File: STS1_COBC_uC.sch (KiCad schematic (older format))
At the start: 27 parts

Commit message: RF modules added + some tweaking on STM32
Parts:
- removed D? (x6): LED, symbol Device:LED
- removed R? (x6): 52.5, symbol Device:R
- added C? (x2): 4.7u, symbol Device:C
- added C? (x5): 100n, symbol Device:C
- added C? (x2): 20p, symbol Device:C
- added C?: 1u, symbol Device:C
- added J? (x8): Conn_01x01_Male, symbol Connector:Conn_01x01_Male
- added JP?: Jumper_NC_Dual, symbol Device:Jumper_NC_Dual
- added R?: 220, symbol Device:R
- added Y?: 12MHz, symbol Device:Crystal
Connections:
- net labels added: GND, SPI1_CLK, SPI1_MISO, SPI1_MOSI, SPI2_CLK, SPI2_MISO, SPI2_MOSI, SPI3_MISO, SPI3_MOSI, SPI3_NSS, SPI3_SCLK, STM32_PowerSupply1, STM32_PowerSupply2, STM32_PowerSupply3, STM32_PowerSupply4
- net labels removed: Earth
- wire segments 41 -> 113
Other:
- note added: "Boot0 / Boot1 Bootloaderconfig\n"
- note added: "PA4 SPI3 NSS\nPA5 SPI1 SCLK\nPA6 SPI1 MISO\nPA7 SPI1 MOSI\nPA13 SWDIO\nPA14 SWCLK\nPB12 SPI3 SCKL\nPC2 SPI2 MISO\nPC3 SPI2 MOSI\nPC7 SPI2 SCLK\nPC11 SPI3 MISO\nPC12 SPI3 MOSI\n\nunbedingt spis wegen nss prüfen\n"
- note added: "Will be connected via jumpers\n"
- note removed: "PA5 SPI1 SCLK\nPA6 SPI1 MISO\nPA7 SPI1 MOSI\nPA13 SWDIO\nPA14 SWCLK\nPC2 SPI2 MISO\nPC3 SPI2 MOSI\nPC7 SPI2 SCLK\n\n"
- moved on the sheet: D?, J?, R?

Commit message: finished schematic
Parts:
- removed J? (x2): Conn_01x02_Female, symbol Connector:Conn_01x02_Female
- added J11, J15, J19, J22, J4: Conn_01x01_Male, symbol Connector:Conn_01x01_Male
- added J2: Conn_01x05_Female, Connector_PinHeader_2.54mm:PinHeader_1x05_P2.54mm_Horizontal, symbol Connector:Conn_01x05_Female
- C1, C10, C2, C3, C4, C5, C6, C7, C8, C9: renamed from C?; footprint (none) -> Capacitor_SMD:C_0805_2012Metric
- D1, D2: renamed from D?; footprint (none) -> LED_SMD:LED_0805_2012Metric
- IC1: renamed from IC?; footprint QFP50P1200X1200X160-64N -> STM32F411RET6TR:QFP50P1200X1200X160-64N
- R2, R3: renamed from R?; value 52.5 -> 100
- gave numbers to parts that had none: 19
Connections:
- net GND: now also J2.3 (Pin_3); no longer J7.1 (Pin_1)
- net SPI3_SCLK: now also IC1.51 (PC10), J15.1 (Pin_1); no longer IC1.33 (PB12), J20.1 (Pin_1)
- net STM32_PowerSupply4: now also J2.1 (Pin_1)
- net SPI4_MOSI: now reaches IC1.15 (PA1)
- net SPI4_MOSI: now also J4.1 (Pin_1)
- net STM32_PowerSupply1: now reaches C5.2, IC1.19 (VDD_1)
- net STM32_PowerSupply1: now also J7.1 (Pin_1)
- net SPI4_SCLK: now reaches IC1.34 (PB13)
- net SPI4_SCLK: now also J19.1 (Pin_1)
- net STM32_PA9(Watchdog_toggle): now reaches IC1.42 (PA9)
- net SPI4_MISO: now reaches IC1.44 (PA11)
- net SPI4_MISO: now also J22.1 (Pin_1)
- net at IC1.46 (PA13), J23.1 (Pin_1), R3.2: now also J2.4 (Pin_4)
- net at IC1.49 (PA14), J17.1 (Pin_1), R2.2: now also J2.2 (Pin_2)
- net SPI2_NSS: now reaches IC1.62 (PB9)
- net SPI2_NSS: now also J11.1 (Pin_1)
- net STM32_NRST: now reaches IC1.7 (NRST)
- net STM32_NRST: now also J2.5 (Pin_5)
- new net SPI4_NSS: IC1.33 (PB12), J20.1 (Pin_1)
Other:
- note added: "PA1 SPI4 MOSI\nPA4 SPI3 NSS\nPA5 SPI1 SCLK\nPA6 SPI1 MISO\nPA7 SPI1 MOSI\nPA11 SPI4 MISO\nPA13 SWDIO\nPA14 SWCLK\nPB9 SPI2 NSS\nPB12 SPI4 NSS\nPB13 SPI4 SCLK\nPC2 SPI2 MISO\nPC3 SPI2 MOSI\nPC7 SPI2 SCLK\nPC10 SPI3 SCLK\nPC11 SPI3 MISO\nPC12 SPI3 MOSI\n\nunbedingt spis wegen nss prüfen\n"
- note removed: "PA4 SPI3 NSS\nPA5 SPI1 SCLK\nPA6 SPI1 MISO\nPA7 SPI1 MOSI\nPA13 SWDIO\nPA14 SWCLK\nPB12 SPI3 SCKL\nPC2 SPI2 MISO\nPC3 SPI2 MOSI\nPC7 SPI2 SCLK\nPC11 SPI3 MISO\nPC12 SPI3 MOSI\n\nunbedingt spis wegen nss prüfen\n"

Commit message: new template
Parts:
- J10, J11, J12, J13, J14, J15, J16, J17, J18, J19, J20, J21, J22, J23, J3, J4, J5, J6, J7, J8, J9: footprint (none) -> Connector_PinHeader_2.54mm:PinHeader_1x01_P2.54mm_Vertical
- R1, R2, R3: footprint (none) -> Resistor_SMD:R_0805_2012Metric
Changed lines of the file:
@@
 F 0 "J5" V 4612 3794 50  0000 L CNN
 F 1 "Conn_01x01_Male" V 4703 3794 50  0000 L CNN
-F 2 "" H 4550 3750 50  0001 C CNN
+F 2 "Connector_PinHeader_2.54mm:PinHeader_1x01_P2.54mm_Vertical" H 4550 3750 50  0001 C CNN
 F 3 "~" H 4550 3750 50  0001 C CNN
 	1    4550 3750
@@
 F 0 "J6" V 4704 4162 50  0000 R CNN
 F 1 "Conn_01x01_Male" V 4613 4162 50  0000 R CNN
-F 2 "" H 4550 4250 50  0001 C CNN
+F 2 "Connector_PinHeader_2.54mm:PinHeader_1x01_P2.54mm_Vertical" H 4550 4250 50  0001 C CNN
 F 3 "~" H 4550 4250 50  0001 C CNN
 	1    4550 4250
@@
 F 0 "J9" H 5408 5681 50  0000 C CNN
 F 1 "Conn_01x01_Male" H 5408 5590 50  0000 C CNN
-F 2 "" H 5300 5500 50  0001 C CNN
+F 2 "Connector_PinHeader_2.54mm:PinHeader_1x01_P2.54mm_Vertical" H 5300 5500 50  0001 C CNN
 F 3 "~" H 5300 5500 50  0001 C CNN
 	1    5300 5500
@@
 F 0 "J10" H 5508 5831 50  0000 C CNN
 F 1 "Conn_01x01_Male" H 5508 5740 50  0000 C CNN
-F 2 "" H 5400 5650 50  0001 C CNN
+F 2 "Connector_PinHeader_2.54mm:PinHeader_1x01_P2.54mm_Vertical" H 5400 5650 50  0001 C CNN
 F 3 "~" H 5400 5650 50  0001 C CNN
 	1    5400 5650
@@
 F 0 "J12" H 5872 5482 50  0000 R CNN
 F 1 "Conn_01x01_Male" H 6200 5600 50  0000 R CNN
-F 2 "" H 5900 5550 50  0001 C CNN
+F 2 "Connector_PinHeader_2.54mm:PinHeader_1x01_P2.54mm_Vertical" H 5900 5550 50  0001 C CNN
 F 3 "~" H 5900 5550 50  0001 C CNN
 	1    5900 5550
@@
 F 0 "J21" V 7262 3894 50  0000 L CNN
 F 1 "Conn_01x01_Male" V 7353 3894 50  0000 L CNN
-F 2 "" H 7200 3850 50  0001 C CNN
+F 2 "Connector_PinHeader_2.54mm:PinHeader_1x01_P2.54mm_Vertical" H 7200 3850 50  0001 C CNN
 F 3 "~" H 7200 3850 50  0001 C CNN
 	1    7200 3850
@@
 F 0 "J23" V 7462 2944 50  0000 L CNN
 F 1 "Conn_01x01_Male" V 7553 2944 50  0000 L CNN
-F 2 "" H 7400 2900 50  0001 C CNN
+F 2 "Connector_PinHeader_2.54mm:PinHeader_1x01_P2.54mm_Vertical" H 7400 2900 50  0001 C CNN
 F 3 "~" H 7400 2900 50  0001 C CNN
 	1    7400 2900
@@
 F 0 "J17" H 6772 2182 50  0000 R CNN
 F 1 "Conn_01x01_Male" V 6750 2600 50  0000 R CNN
-F 2 "" H 6800 2250 50  0001 C CNN
+F 2 "Connector_PinHeader_2.54mm:PinHeader_1x01_P2.54mm_Vertical" H 6800 2250 50  0001 C CNN
 F 3 "~" H 6800 2250 50  0001 C CNN
 	1    6800 2250
@@
 F 0 "R2" H 6650 2000 50  0000 L CNN
 F 1 "100" V 6600 1900 50  0000 L CNN
-F 2 "" V 6530 2000 50  0001 C CNN
+F 2 "Resistor_SMD:R_0805_2012Metric" V 6530 2000 50  0001 C CNN
 F 3 "~" H 6600 2000 50  0001 C CNN
 	1    6600 2000
@@
 F 0 "R3" H 7820 2996 50  0000 L CNN
 F 1 "100" H 7820 2905 50  0000 L CNN
-F 2 "" V 7680 2950 50  0001 C CNN
+F 2 "Resistor_SMD:R_0805_2012Metric" V 7680 2950 50  0001 C CNN
 F 3 "~" H 7750 2950 50  0001 C CNN
 	1    7750 2950
@@
 F 0 "J7" H 4908 5681 50  0000 C CNN
 F 1 "Conn_01x01_Male" H 4908 5590 50  0000 C CNN
-F 2 "" H 4800 5500 50  0001 C CNN
+F 2 "Connector_PinHeader_2.54mm:PinHeader_1x01_P2.54mm_Vertical" H 4800 5500 50  0001 C CNN
 F 3 "~" H 4800 5500 50  0001 C CNN
 	1    4800 5500
@@
 F 0 "J18" H 7050 5600 50  0000 C CNN
 F 1 "Conn_01x01_Male" H 6650 5600 50  0000 C CNN
-F 2 "" H 7000 5600 50  0001 C CNN
+F 2 "Connector_PinHeader_2.54mm:PinHeader_1x01_P2.54mm_Vertical" H 7000 5600 50  0001 C CNN
 F 3 "~" H 7000 5600 50  0001 C CNN
 	1    7000 5600
@@
 F 0 "J16" V 6812 2894 50  0000 L CNN
 F 1 "Conn_01x01_Male" V 6750 2750 50  0000 L CNN
-F 2 "" H 6750 2850 50  0001 C CNN
+F 2 "Connector_PinHeader_2.54mm:PinHeader_1x01_P2.54mm_Vertical" H 6750 2850 50  0001 C CNN
 F 3 "~" H 6750 2850 50  0001 C CNN
 	1    6750 2850
@@
 F 0 "J8" H 4872 2032 50  0000 R CNN
 F 1 "Conn_01x01_Male" H 4872 2123 50  0000 R CNN
-F 2 "" H 4900 2100 50  0001 C CNN
+F 2 "Connector_PinHeader_2.54mm:PinHeader_1x01_P2.54mm_Vertical" H 4900 2100 50  0001 C CNN
 F 3 "~" H 4900 2100 50  0001 C CNN
 	1    4900 2100
@@
 F 0 "R1" H 3220 3796 50  0000 L CNN
 F 1 "220" V 3150 3650 50  0000 L CNN
-F 2 "" V 3080 3750 50  0001 C CNN
+F 2 "Resistor_SMD:R_0805_2012Metric" V 3080 3750 50  0001 C CNN
 F 3 "~" H 3150 3750 50  0001 C CNN
 	1    3150 3750
@@
 F 0 "J14" H 6072 2182 50  0000 R CNN
 F 1 "Conn_01x01_Male" H 6072 2273 50  0000 R CNN
-F 2 "" H 6100 2250 50  0001 C CNN
+F 2 "Connector_PinHeader_2.54mm:PinHeader_1x01_P2.54mm_Vertical" H 6100 2250 50  0001 C CNN
 F 3 "~" H 6100 2250 50  0001 C CNN
 	1    6100 2250
@@
 F 0 "J13" H 5972 2132 50  0000 R CNN
 F 1 "Conn_01x01_Male" H 5972 2223 50  0000 R CNN
-F 2 "" H 6000 2200 50  0001 C CNN
+F 2 "Connector_PinHeader_2.54mm:PinHeader_1x01_P2.54mm_Vertical" H 6000 2200 50  0001 C CNN
 F 3 "~" H 6000 2200 50  0001 C CNN
 	1    6000 2200
@@
 F 0 "J20" V 7112 4794 50  0000 L CNN
 F 1 "Conn_01x01_Male" V 7203 4794 50  0000 L CNN
-F 2 "" H 7050 4750 50  0001 C CNN
+F 2 "Connector_PinHeader_2.54mm:PinHeader_1x01_P2.54mm_Vertical" H 7050 4750 50  0001 C CNN
 F 3 "~" H 7050 4750 50  0001 C CNN
 	1    7050 4750
@@
 F 0 "J3" H 4508 6181 50  0000 C CNN
 F 1 "Conn_01x01_Male" H 4508 6090 50  0000 C CNN
-F 2 "" H 4400 6000 50  0001 C CNN
+F 2 "Connector_PinHeader_2.54mm:PinHeader_1x01_P2.54mm_Vertical" H 4400 6000 50  0001 C CNN
 F 3 "~" H 4400 6000 50  0001 C CNN
 	1    4400 6000
@@
 F 0 "J4" H 4608 5081 50  0000 C CNN
 F 1 "Conn_01x01_Male" H 4550 4900 50  0000 C CNN
-F 2 "" H 4500 4900 50  0001 C CNN
+F 2 "Connector_PinHeader_2.54mm:PinHeader_1x01_P2.54mm_Vertical" H 4500 4900 50  0001 C CNN
 F 3 "~" H 4500 4900 50  0001 C CNN
 	1    4500 4900
@@
 F 0 "J22" V 7362 3294 50  0000 L CNN
 F 1 "Conn_01x01_Male" V 7453 3294 50  0000 L CNN
-F 2 "" H 7300 3250 50  0001 C CNN
+F 2 "Connector_PinHeader_2.54mm:PinHeader_1x01_P2.54mm_Vertical" H 7300 3250 50  0001 C CNN
 F 3 "~" H 7300 3250 50  0001 C CNN
 	1    7300 3250
@@
 F 0 "J11" V 5562 2094 50  0000 L CNN
 F 1 "Conn_01x01_Male" V 5653 2094 50  0000 L CNN
-F 2 "" H 5500 2050 50  0001 C CNN
+F 2 "Connector_PinHeader_2.54mm:PinHeader_1x01_P2.54mm_Vertical" H 5500 2050 50  0001 C CNN
 F 3 "~" H 5500 2050 50  0001 C CNN
 	1    5500 2050
@@
 F 0 "J19" V 7112 4294 50  0000 L CNN
 F 1 "Conn_01x01_Male" V 7203 4294 50  0000 L CNN
-F 2 "" H 7050 4250 50  0001 C CNN
+F 2 "Connector_PinHeader_2.54mm:PinHeader_1x01_P2.54mm_Vertical" H 7050 4250 50  0001 C CNN
 F 3 "~" H 7050 4250 50  0001 C CNN
 	1    7050 4250
@@
 F 0 "J15" H 6172 2082 50  0000 R CNN
 F 1 "Conn_01x01_Male" H 6172 2173 50  0000 R CNN
-F 2 "" H 6200 2150 50  0001 C CNN
+F 2 "Connector_PinHeader_2.54mm:PinHeader_1x01_P2.54mm_Vertical" H 6200 2150 50  0001 C CNN
 F 3 "~" H 6200 2150 50  0001 C CNN
 	1    6200 2150
@@
 	6400 2150 6400 2350
 Connection ~ 6400 2150
-Text HLabel 4550 3650 0    50   Input ~ 0
-STM32_NRST
 Text HLabel 8400 3650 2    50   Input ~ 0
 STM32_PA9(Watchdog_toggle)
@@
 Wire Wire Line
 	4650 3650 4550 3650
+Text HLabel 4550 3650 0    50   Input ~ 0
+STM32_NRST
 $EndSCHEMATC

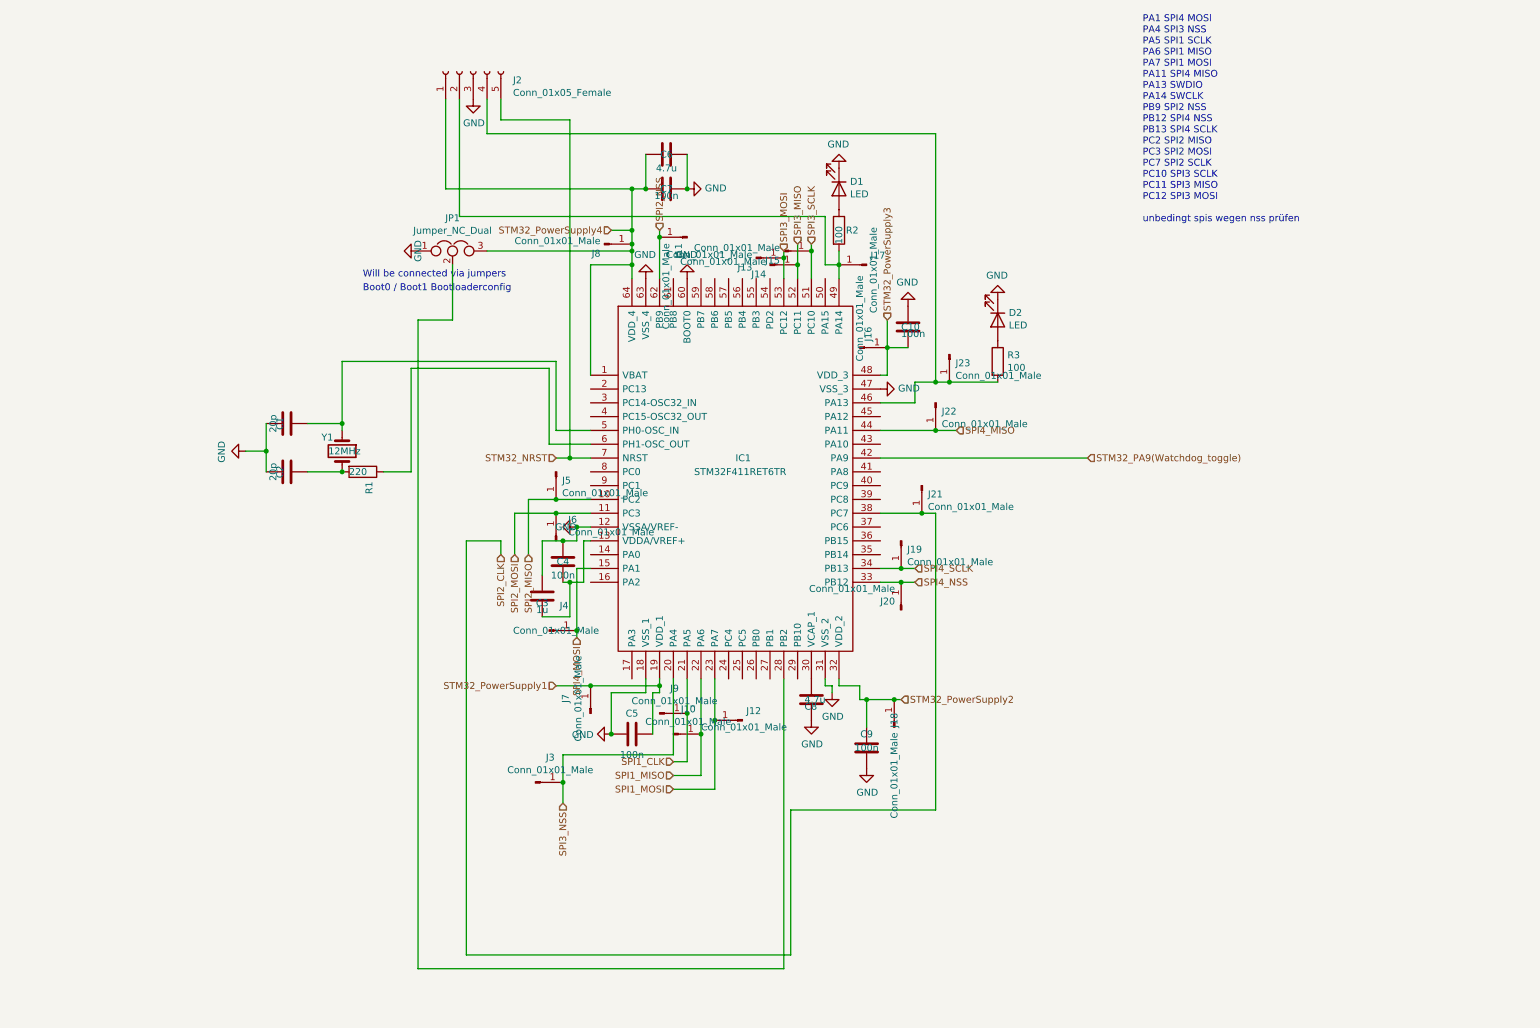
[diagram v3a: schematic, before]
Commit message: BuckBoost added
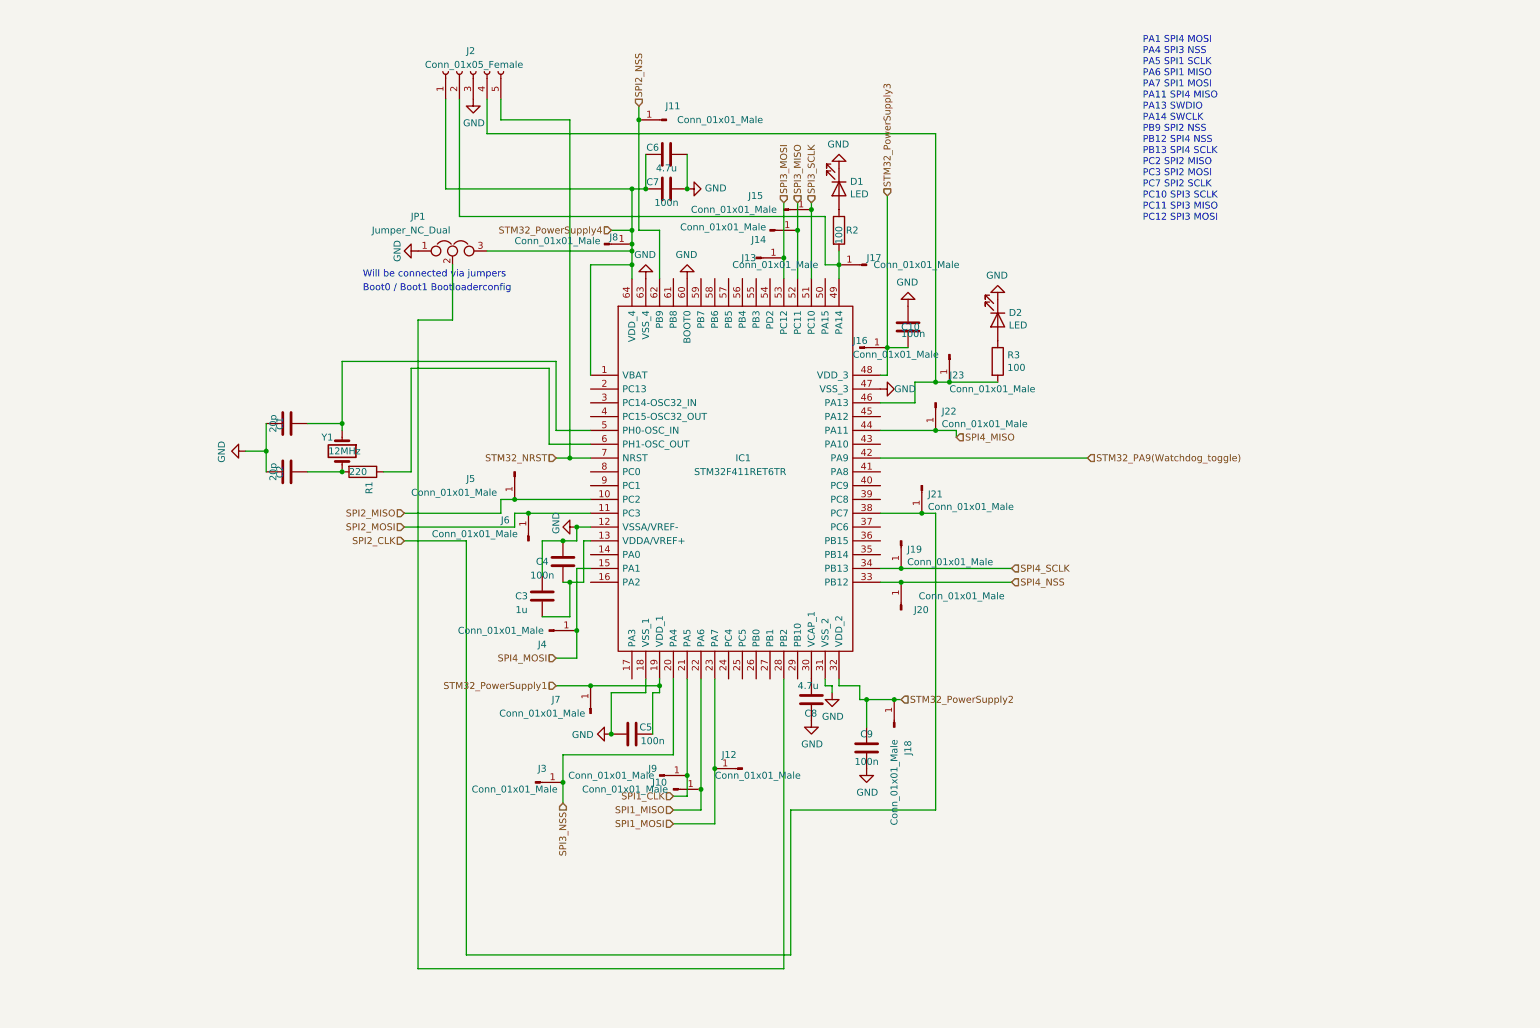
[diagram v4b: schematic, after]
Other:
- note added: "PA1 SPI4 MOSI\nPA4 SPI3 NSS\nPA5 SPI1 SCLK\nPA6 SPI1 MISO\nPA7 SPI1 MOSI\nPA11 SPI4 MISO\nPA13 SWDIO\nPA14 SWCLK\nPB9 SPI2 NSS\nPB12 SPI4 NSS\nPB13 SPI4 SCLK\nPC2 SPI2 MISO\nPC3 SPI2 MOSI\nPC7 SPI2 SCLK\nPC10 SPI3 SCLK\nPC11 SPI3 MISO\nPC12 SPI3 MOSI\n\n\n"
- note removed: "PA1 SPI4 MOSI\nPA4 SPI3 NSS\nPA5 SPI1 SCLK\nPA6 SPI1 MISO\nPA7 SPI1 MOSI\nPA11 SPI4 MISO\nPA13 SWDIO\nPA14 SWCLK\nPB9 SPI2 NSS\nPB12 SPI4 NSS\nPB13 SPI4 SCLK\nPC2 SPI2 MISO\nPC3 SPI2 MOSI\nPC7 SPI2 SCLK\nPC10 SPI3 SCLK\nPC11 SPI3 MISO\nPC12 SPI3 MOSI\n\nunbedingt spis wegen nss prüfen\n"
- moved on the sheet: J10, J11, J12, J14, J15, J5, J6, J9

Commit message: schematic done
final tweaks (adding LEDS, pin headers, moving circuits...)
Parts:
- added C?: 100n, Capacitor_SMD:C_0805_2012Metric, symbol Device:C
- added C?: 47u, Capacitor_SMD:C_0805_2012Metric, symbol Device:C
- added D?: LED, LED_SMD:LED_0805_2012Metric, symbol Device:LED
- added IC?: STWD100PYW83F, SamacSys_Parts:SOT65P210X110-5N, symbol SamacSys_Parts:STWD100PYW83F
- added J1, J26, J27, J28, J29, J30, J31, J32, J33, J34, J35, J36, J37, J38, J? (x15): Conn_01x01_Male, Connector_PinHeader_2.54mm:PinHeader_1x01_P2.54mm_Vertical, symbol Connector:Conn_01x01_Male
- added R?: 4k7, Resistor_SMD:R_0805_2012Metric, symbol Device:R
- added R?: 100, Resistor_SMD:R_0805_2012Metric, symbol Device:R
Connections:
- net GND: now also C?.2, C?.2, D?.1 (K), IC?.2 (GND), IC?.3 (~EN)
- net STM32_NRST: now also R?.2
- net STM32_PA9(Watchdog_toggle): now also IC?.4 (WDI), J?.1 (Pin_1)
- net at IC1.16 (PA2): now also J1.1 (Pin_1)
- net at IC1.17 (PA3): now also J26.1 (Pin_1)
- net PC13: now reaches IC1.2 (PC13)
- net PC13: now also J?.1 (Pin_1)
- net Flash_WP: now reaches IC1.24 (PC4)
- net at IC1.25 (PC5): now also J27.1 (Pin_1)
- net at IC1.26 (PB0): now also J28.1 (Pin_1)
- net at IC1.27 (PB1): now also J29.1 (Pin_1)
- net at IC1.29 (PB10): now also J30.1 (Pin_1)
- net PC14: now reaches IC1.3 (PC14-OSC32_IN)
- net PC14: now also J?.1 (Pin_1)
- net at IC1.35 (PB14): now also J38.1 (Pin_1)
- net at IC1.36 (PB15): now also J37.1 (Pin_1)
- net at IC1.37 (PC6): now also J36.1 (Pin_1)
- net at IC1.39 (PC8): now also J35.1 (Pin_1)
- net PC15: now reaches IC1.4 (PC15-OSC32_OUT)
- net PC15: now also J?.1 (Pin_1)
- net at IC1.40 (PC9): now also J34.1 (Pin_1)
- net at IC1.41 (PA8): now also J33.1 (Pin_1)
- net at IC1.43 (PA10): now also J32.1 (Pin_1)
- net at IC1.45 (PA12): now also J31.1 (Pin_1)
- net PA15: now reaches IC1.50 (PA15)
- net PA15: now also J?.1 (Pin_1)
- net PD2: now reaches IC1.54 (PD2)
- net PD2: now also J?.1 (Pin_1)
- net PB3: now reaches IC1.55 (PB3)
- net PB3: now also J?.1 (Pin_1)
- net PB4: now reaches IC1.56 (PB4)
- net PB4: now also J?.1 (Pin_1)
- net PB5: now reaches IC1.57 (PB5)
- net PB5: now also J?.1 (Pin_1)
- net PB6: now reaches IC1.58 (PB6)
- net PB6: now also J?.1 (Pin_1)
- net PB7: now reaches IC1.59 (PB7)
- net PB7: now also J?.1 (Pin_1)
- net PB9: now reaches IC1.61 (PB8)
- net PB9: now also J?.1 (Pin_1)
- net PC0: now reaches IC1.8 (PC0)
- net PC0: now also J?.1 (Pin_1)
- net PC1: now reaches IC1.9 (PC1)
- net PC1: now also J?.1 (Pin_1)
- new net: IC?.1 (~WDO), R?.1
- new net: D?.2 (A), R?.1
- new net Watchdog_VCC: C?.1, C?.1, IC?.5 (VCC), J?.1 (Pin_1), R?.2
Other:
- note added: "PA1 SPI4 MOSI\nPA4 SPI3 NSS\nPA5 SPI1 SCLK\nPA6 SPI1 MISO\nPA7 SPI1 MOSI\nPA11 SPI4 MISO\nPA13 SWDIO\nPA14 SWCLK\nPB9 SPI2 NSS\nPB12 SPI4 NSS\nPB13 SPI4 SCLK\nPC2 SPI2 MISO\nPC3 SPI2 MOSI\nPC7 SPI2 SCLK\nPC10 SPI3 SCLK\nPC11 SPI3 MISO\nPC12 SPI3 MOSI\n\n\n\n"
- note added: "WDI needs to be toggled during WTP if not WDO is asserted\n"
- note removed: "PA1 SPI4 MOSI\nPA4 SPI3 NSS\nPA5 SPI1 SCLK\nPA6 SPI1 MISO\nPA7 SPI1 MOSI\nPA11 SPI4 MISO\nPA13 SWDIO\nPA14 SWCLK\nPB9 SPI2 NSS\nPB12 SPI4 NSS\nPB13 SPI4 SCLK\nPC2 SPI2 MISO\nPC3 SPI2 MOSI\nPC7 SPI2 SCLK\nPC10 SPI3 SCLK\nPC11 SPI3 MISO\nPC12 SPI3 MOSI\n\n\n"
- moved on the sheet: J13, J19, J21, J22

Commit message: Issues removed + further layout development
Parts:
- added C32: 100n, Capacitor_SMD:C_0805_2012Metric, symbol Device:C
- JP1: footprint (none) -> Connector_PinHeader_2.54mm:PinHeader_1x03_P2.54mm_Vertical
- gave numbers to parts that had none: 21
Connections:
- net STM32_PowerSupply1 is gone; now on net +3V3: C5.2, IC1.19 (VDD_1), J7.1 (Pin_1)
- net STM32_PowerSupply2 is gone; now on net +3V3: C9.1, IC1.32 (VDD_2), J18.1 (Pin_1)
- net STM32_PowerSupply3 is gone; now on net +3V3: C10.1, IC1.48 (VDD_3), J16.1 (Pin_1)
- net STM32_PowerSupply4 is gone; now on net +3V3: C6.2, C7.2, IC1.1 (VBAT), IC1.64 (VDD_4), J2.1 (Pin_1), J8.1 (Pin_1), JP1.3
- net GND: now also IC1.28 (PB2), C32.1; no longer IC1.60 (BOOT0)
- net STM32_NRST: now also C32.2
- net +3V3: now reaches C3.1, C4.2, IC1.13 (VDDA/VREF+)
- net at JP1.2: now also IC1.60 (BOOT0); no longer IC1.28 (PB2)
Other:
- note added: "PA1 SPI4 MOSI\nPA4 SPI3 NSS\nPA5 SPI1 SCLK\nPA6 SPI1 MISO\nPA7 SPI1 MOSI\nPA11 SPI4 MISO\nPA13 SWDIO\nPA14 SWCLK\nPB2 BOOT1\nPB9 SPI2 NSS\nPB12 SPI4 NSS\nPB13 SPI4 SCLK\nPC2 SPI2 MISO\nPC3 SPI2 MOSI\nPC7 SPI2 SCLK\nPC10 SPI3 SCLK\nPC11 SPI3 MISO\nPC12 SPI3 MOSI\n\n\n\n"
- note removed: "PA1 SPI4 MOSI\nPA4 SPI3 NSS\nPA5 SPI1 SCLK\nPA6 SPI1 MISO\nPA7 SPI1 MOSI\nPA11 SPI4 MISO\nPA13 SWDIO\nPA14 SWCLK\nPB9 SPI2 NSS\nPB12 SPI4 NSS\nPB13 SPI4 SCLK\nPC2 SPI2 MISO\nPC3 SPI2 MOSI\nPC7 SPI2 SCLK\nPC10 SPI3 SCLK\nPC11 SPI3 MISO\nPC12 SPI3 MOSI\n\n\n\n"
- moved on the sheet: J4
